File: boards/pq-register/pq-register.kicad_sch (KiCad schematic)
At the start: 48 parts, among them P1 Card Edge, Q51 T1-N652, Q52 T1-N652, Q53 T1-N652, Q54 T1-N652, Q55 T1-N652, Q56 T1-N652, Q97 T1-N652, Q98 T1-N652, Q99 T1-N652

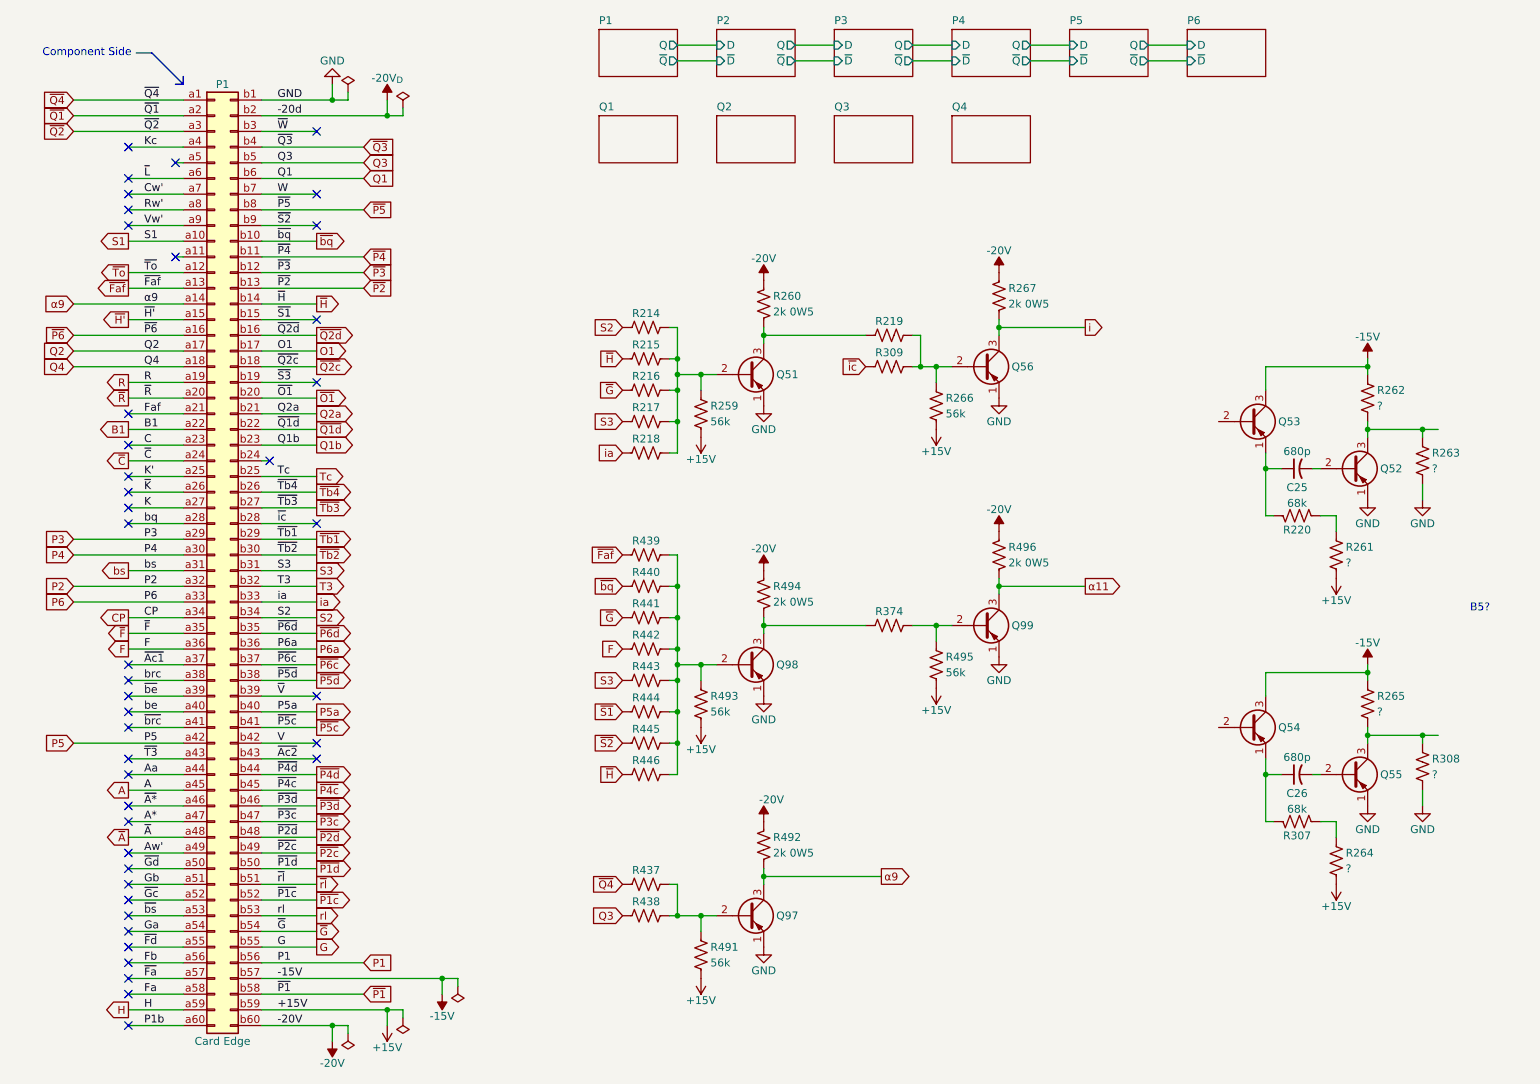
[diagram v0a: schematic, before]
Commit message: Run ERC and clean up P & Q Register board.
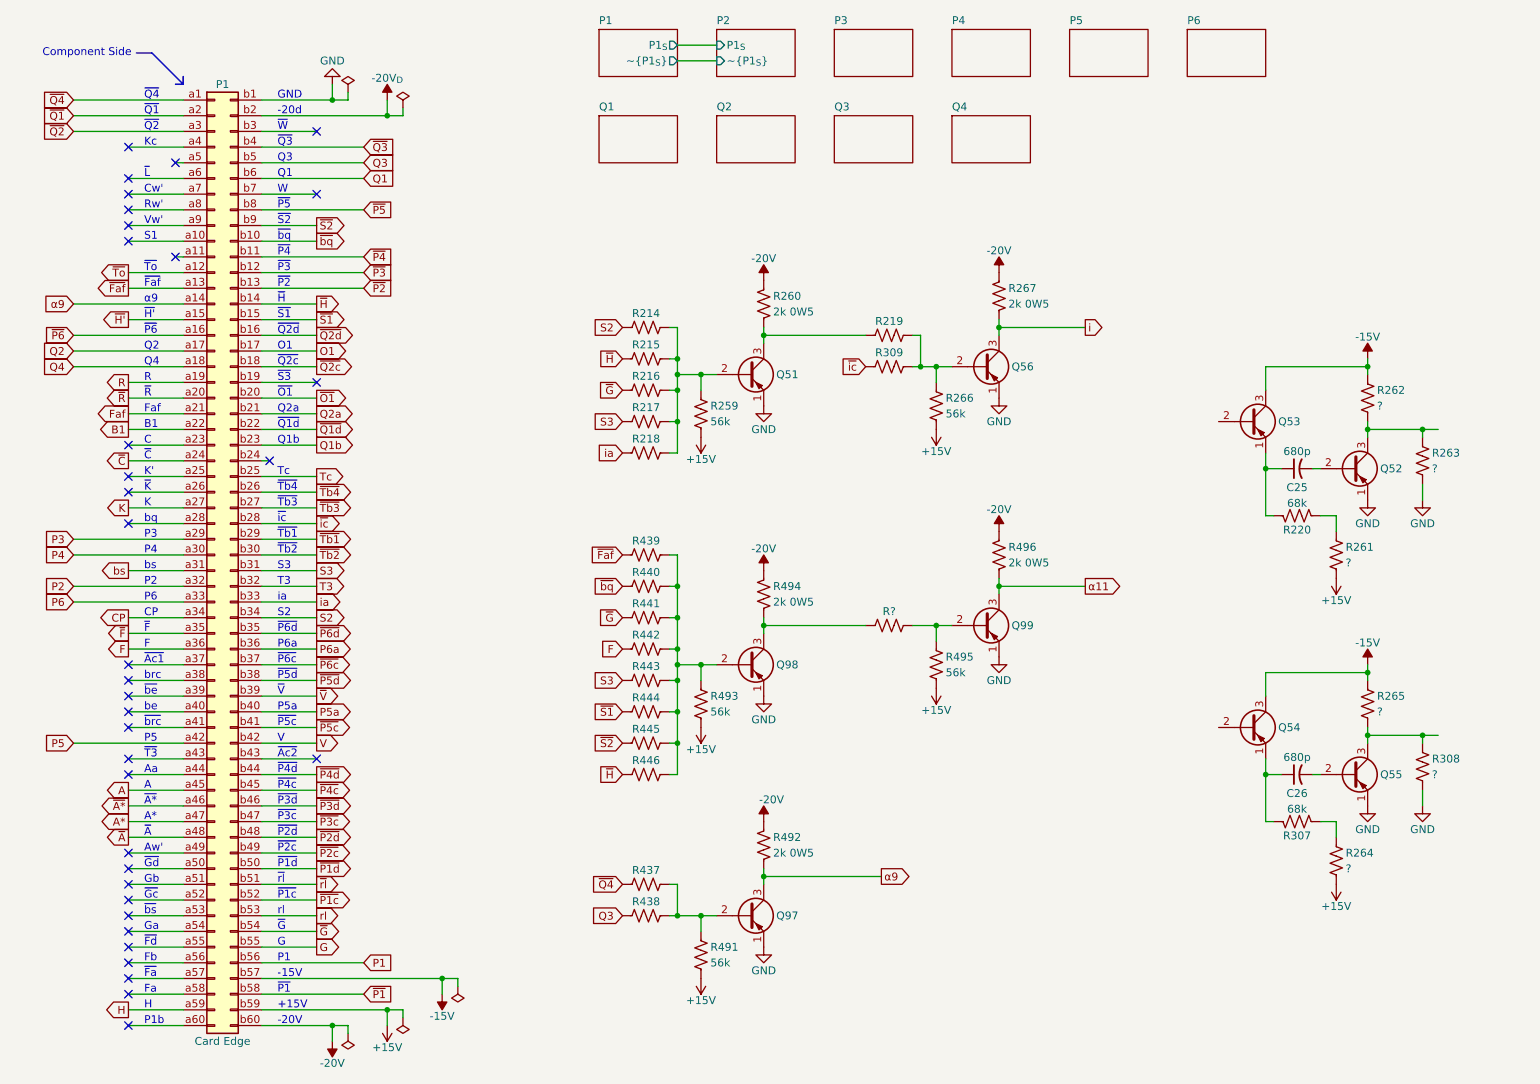
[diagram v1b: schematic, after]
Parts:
- renumbered R374 to R?
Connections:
- net Aa: no longer names the net of P1.a44 (Pin_a44)
- net Aw': no longer names the net of P1.a49 (Pin_a49)
- net C: no longer names the net of P1.a23 (Pin_a23)
- net Cw': no longer names the net of P1.a7 (Pin_a7)
- net Fa: no longer names the net of P1.a58 (Pin_a58)
- net Fb: no longer names the net of P1.a56 (Pin_a56)
- net Ga: no longer names the net of P1.a54 (Pin_a54)
- net Gb: no longer names the net of P1.a51 (Pin_a51)
- net K': no longer names the net of P1.a25 (Pin_a25)
- net Kc: no longer names the net of P1.a4 (Pin_a4)
- net P1b: no longer names the net of P1.a60 (Pin_a60)
- net Rw': no longer names the net of P1.a8 (Pin_a8)
- net S1: no longer names the net of P1.a10 (Pin_a10)
- net Vw': no longer names the net of P1.a9 (Pin_a9)
- net W: no longer names the net of P1.b7 (Pin_b7)
- net be: no longer names the net of P1.a40 (Pin_a40)
- net bq: no longer names the net of P1.a28 (Pin_a28)
- net brc: no longer names the net of P1.a38 (Pin_a38)
- net ~{Ac1}: no longer names the net of P1.a37 (Pin_a37)
- net ~{Ac2}: no longer names the net of P1.b43 (Pin_b43)
- net ~{Fa}: no longer names the net of P1.a57 (Pin_a57)
- net ~{Fd}: no longer names the net of P1.a55 (Pin_a55)
- net ~{Gc}: no longer names the net of P1.a52 (Pin_a52)
- net ~{Gd}: no longer names the net of P1.a50 (Pin_a50)
- net ~{K}: no longer names the net of P1.a26 (Pin_a26)
- net ~{L}: no longer names the net of P1.a6 (Pin_a6)
- net ~{S3}: no longer names the net of P1.b19 (Pin_b19)
- net ~{T3}: no longer names the net of P1.a43 (Pin_a43)
- net ~{W}: no longer names the net of P1.b3 (Pin_b3)
- net ~{be}: no longer names the net of P1.a39 (Pin_a39)
- net ~{brc}: no longer names the net of P1.a41 (Pin_a41)
- net ~{bs}: no longer names the net of P1.a53 (Pin_a53)
- no-connect marks 43 -> 35
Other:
- sheet P1 ports: added P1_{S}, ~{P1_{S}}; removed Q, ~{Q}
- sheet P2 ports: added P1_{S}, ~{P1_{S}}; removed D, Q, ~{D}, ~{Q}
- sheet P3 ports: added none; removed D, Q, ~{D}, ~{Q}
- sheet P4 ports: added none; removed D, Q, ~{D}, ~{Q}
- sheet P5 ports: added none; removed D, Q, ~{D}, ~{Q}
- sheet P6 ports: added none; removed D, ~{D}
- note added: "+15V"
- note added: "-15V"
- note added: "-20V"
- note added: "-20d"
- note added: "A"
- note added: "A*"
- note added: "Aa"
- note added: "Aw'"
- note added: "B1"
- note added: "C"
- note added: "CP"
- note added: "Cw'"
- note added: "F"
- note added: "Fa"
- note added: "Faf"
- note added: "Fb"
- note added: "G"
- note added: "GND"
- note added: "Ga"
- note added: "Gb"
- note added: "H"
- note added: "K"
- note added: "K'"
- note added: "Kc"
- note added: "O1"
- note added: "P1"
- note added: "P1b"
- note added: "P2"
- note added: "P3"
- note added: "P4"
- note added: "P5"
- note added: "P5a"
- note added: "P6"
- note added: "P6a"
- note added: "Q1"
- note added: "Q1b"
- note added: "Q2"
- note added: "Q2a"
- note added: "Q3"
- note added: "Q4"
- note added: "R"
- note added: "Rw'"
- note added: "S1"
- note added: "S2"
- note added: "S3"
- note added: "T3"
- note added: "Tc"
- note added: "V"
- note added: "Vw'"
- note added: "W"
- note added: "be"
- note added: "bq"
- note added: "brc"
- note added: "bs"
- note added: "ia"
- note added: "rl"
- note added: "~{A*}"
- note added: "~{Ac1}"
- note added: "~{Ac2}"
- note added: "~{A}"
- note added: "~{C}"
- note added: "~{Faf}"
- note added: "~{Fa}"
- note added: "~{Fd}"
- note added: "~{F}"
- note added: "~{Gc}"
- note added: "~{Gd}"
- note added: "~{G}"
- note added: "~{H'}"
- note added: "~{H}"
- note added: "~{K}"
- note added: "~{L}"
- note added: "~{O1}"
- note added: "~{P1c}"
- note added: "~{P1d}"
- note added: "~{P1}"
- note added: "~{P2c}"
- note added: "~{P2d}"
- note added: "~{P2}"
- note added: "~{P3c}"
- note added: "~{P3d}"
- note added: "~{P3}"
- note added: "~{P4c}"
- note added: "~{P4d}"
- note added: "~{P4}"
- note added: "~{P5c}"
- note added: "~{P5d}"
- note added: "~{P5}"
- note added: "~{P6c}"
- note added: "~{P6d}"
- note added: "~{P6}"
- note added: "~{Q1d}"
- note added: "~{Q1}"
- note added: "~{Q2c}"
- note added: "~{Q2d}"
- note added: "~{Q2}"
- note added: "~{Q3}"
- note added: "~{Q4}"
- note added: "~{R}"
- note added: "~{S1}"
- note added: "~{S2}"
- note added: "~{S3}"
- note added: "~{T3}"
- note added: "~{Tb1}"
- note added: "~{Tb2}"
- note added: "~{Tb3}"
- note added: "~{Tb4}"
- note added: "~{To}"
- note added: "~{V}"
- note added: "~{W}"
- note added: "~{be}"
- note added: "~{bq}"
- note added: "~{brc}"
- note added: "~{bs}"
- note added: "~{ic}"
- note added: "~{rl}"
- note added: "α9"
- note removed: "B5?"

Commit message: Trace the Flex-Tally IO Board schematic.
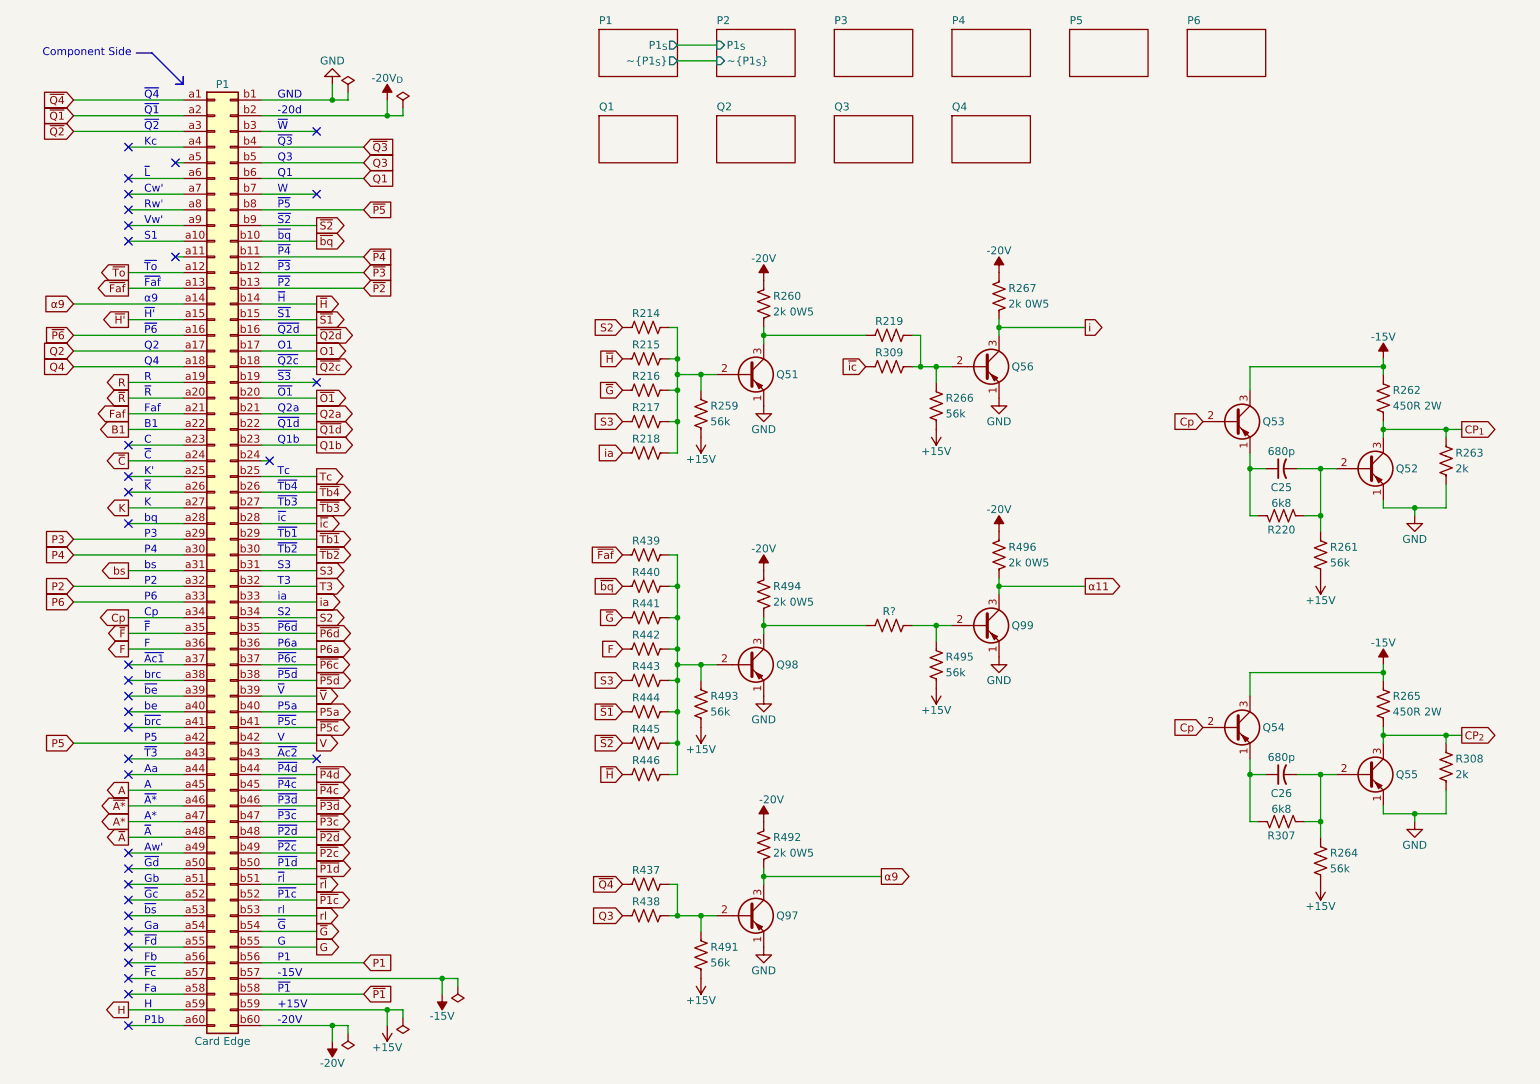
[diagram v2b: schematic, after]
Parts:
- R220, R307: value 68k -> 6k8
- R261, R264: value ? -> 56k
- R262, R265: value ? -> 450R 2W
- R263, R308: value ? -> 2k
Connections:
- net CP is gone; now on net Cp: P1.a34 (Pin_a34)
- net at C26.2, Q55.2 (B): now also R264.1, R307.2
- net at R220.2, R261.1: now also C25.2, Q52.2 (B)
- net Cp: now reaches Q54.2 (B)
- net Cp: now also Q53.2 (B)
- net CP_{2}: now reaches Q55.3 (C), R265.2, R308.1
- net CP_{1}: now reaches Q52.3 (C), R262.2, R263.1
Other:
- note added: "Cp"
- note added: "~{Fc}"
- note removed: "CP"
- note removed: "~{Fa}"
- company: (none) -> © 1962 General Precision; redrawn by Sam Hanes
- moved on the sheet: C25, C26, Q52, Q53, Q54, Q55, R220, R261, R262, R263, R264, R265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
